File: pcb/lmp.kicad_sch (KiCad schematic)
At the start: 6 parts, among them J2 Conn_01x03, J5 TB003-500-P03BE, J6 Conn_01x03_Pin, U2 LMP91000SDX/NOPB

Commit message: Simplify to minimum buck converter components
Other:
- title: (none) -> LMP91000 Portable Potentiostat
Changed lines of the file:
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@@
 	(generator_version "9.0")
 	(paper "A4")
+	(title_block
+		(title "LMP91000 Portable Potentiostat")
+	)
 	(text "Label these with silkscreen"
 		(exclude_from_sim no)

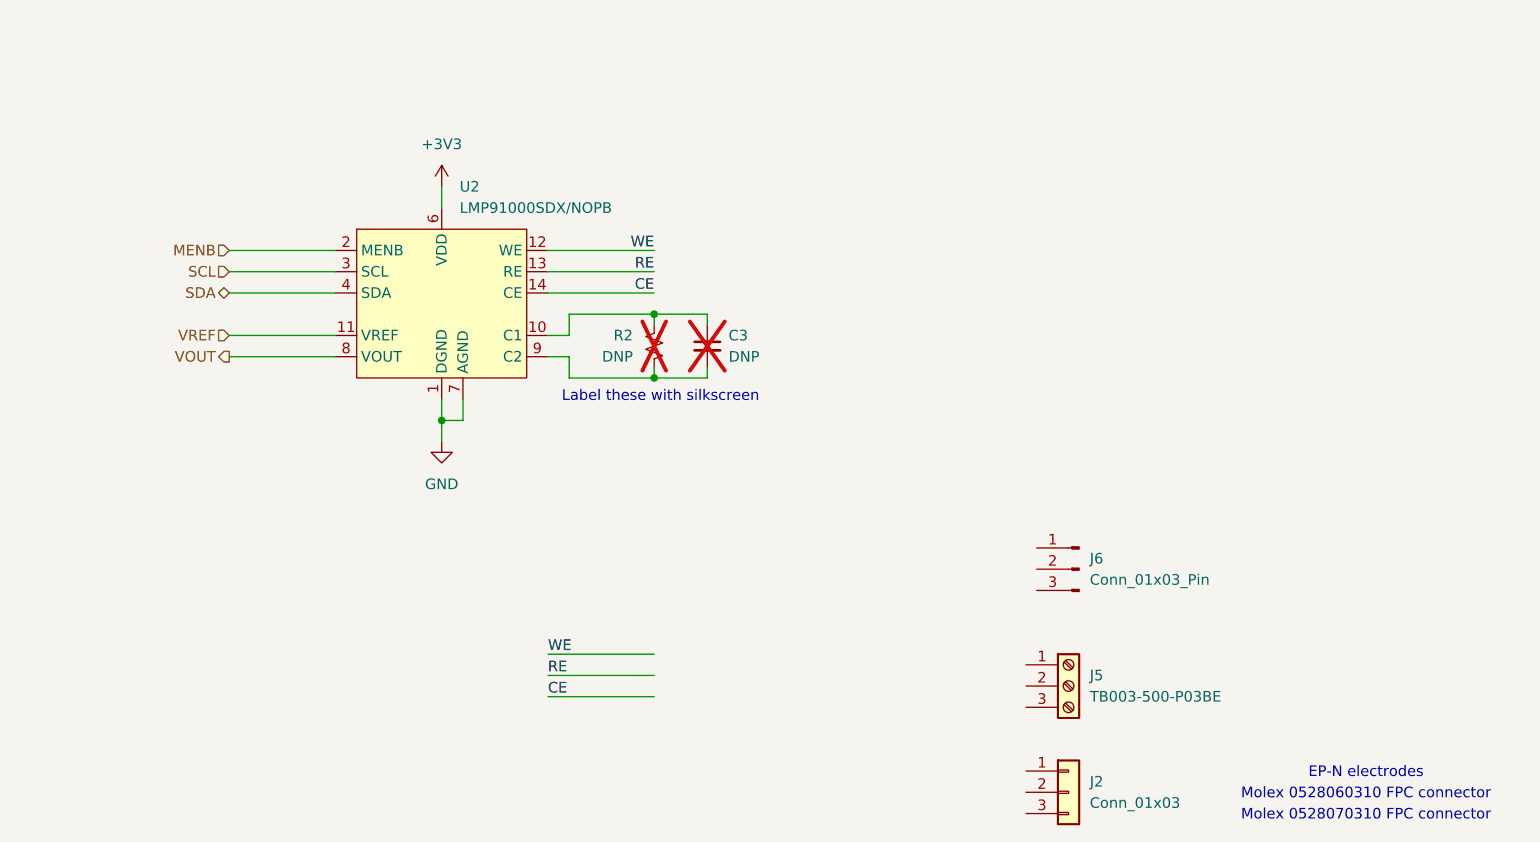
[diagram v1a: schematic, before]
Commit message: Assign footprints, cleanup schematics, start layout
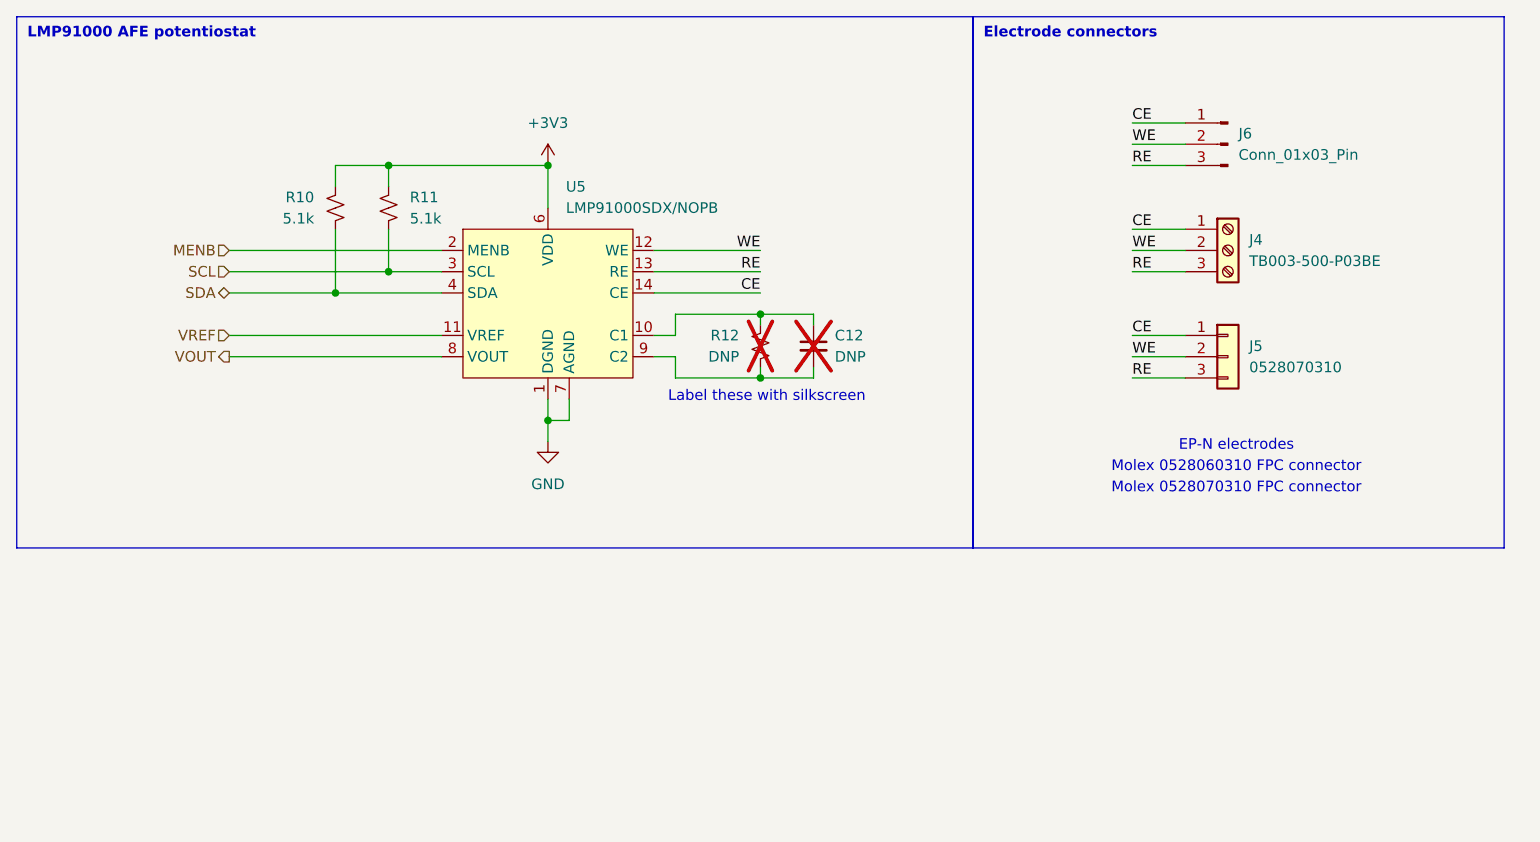
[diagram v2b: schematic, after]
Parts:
- added R10, R11: 5.1k, Resistor_SMD:R_0402_1005Metric, symbol Device:R_Small_US
- C12: renamed from C3; footprint (none) -> Capacitor_SMD:C_0805_2012Metric
- J4: renamed from J5; footprint (none) -> TerminalBlock_SameSky:CUI_TB003-500-P03BE
- J5: renamed from J2; value Conn_01x03 -> 0528070310; footprint (none) -> Connector_Molex_Easy-On:528070310
- J6: footprint (none) -> Connector_PinHeader_2.54mm:PinHeader_1x03_P2.54mm_Vertical; now left out of the parts list
- R12: renamed from R2; footprint (none) -> Resistor_SMD:R_0805_2012Metric
- renumbered U2 to U5
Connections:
- net +3V3: now also R10.2, R11.2
- net CE: now also J4.1 (Pin_1), J5.1 (Pin_1), J6.1 (Pin_1)
- net RE: now also J4.3 (Pin_3), J5.3 (Pin_3), J6.3 (Pin_3)
- net SCL: now also R11.1
- net SDA: now also R10.1
- net WE: now also J4.2 (Pin_2), J5.2 (Pin_2), J6.2 (Pin_2)
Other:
- note added: "Electrode connectors"
- note added: "LMP91000 AFE potentiostat"
- company: (none) -> Clarkson University
- moved on the sheet: C12, J4, J5, J6, R12, U5

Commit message: Finish PCB
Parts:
- C12: footprint Capacitor_SMD:C_0805_2012Metric -> Capacitor_SMD:C_0603_1608Metric_Pad1.08x0.95mm_HandSolder
- J4: value TB003-500-P03BE -> TB0011-350-03GR; footprint TerminalBlock_SameSky:CUI_TB003-500-P03BE -> TerminalBlock_SameSky:SAMESKY_TB0011-350-03GR
- J6: now not fitted
- R12: footprint Resistor_SMD:R_0805_2012Metric -> Resistor_SMD:R_0603_1608Metric_Pad0.98x0.95mm_HandSolder
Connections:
- net CE: now also J4.3 (Pin_3); no longer J4.1 (Pin_1)
- net RE: now also J4.1 (Pin_1); no longer J4.3 (Pin_3)
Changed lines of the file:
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@@
 			)
 		)
-		(property "Footprint" "Resistor_SMD:R_0805_2012Metric"
+		(property "Footprint" "Resistor_SMD:R_0603_1608Metric_Pad0.98x0.95mm_HandSolder"
 			(at 101.6 52.07 0)
 			(effects
@@
 		(lib_id "Connector:Screw_Terminal_01x03")
 		(at 157.48 40.64 0)
+		(mirror x)
 		(unit 1)
 		(exclude_from_sim no)
@@
 		(on_board yes)
 		(dnp no)
-		(fields_autoplaced yes)
 		(property "Reference" "J4"
-			(at 160.02 39.3699 0)
-			(effects
-				(font
-					(size 1.27 1.27)
-				)
-				(justify left)
-			)
-		)
-		(property "Value" "TB003-500-P03BE"
-			(at 160.02 41.9099 0)
-			(effects
-				(font
-					(size 1.27 1.27)
-				)
-				(justify left)
-			)
-		)
-		(property "Footprint" "TerminalBlock_SameSky:CUI_TB003-500-P03BE"
+			(at 160.02 41.9101 0)
+			(effects
+				(font
+					(size 1.27 1.27)
+				)
+				(justify left)
+			)
+		)
+		(property "Value" "TB0011-350-03GR"
+			(at 160.02 39.3701 0)
+			(effects
+				(font
+					(size 1.27 1.27)
+				)
+				(justify left)
+			)
+		)
+		(property "Footprint" "TerminalBlock_SameSky:SAMESKY_TB0011-350-03GR"
 			(at 157.48 40.64 0)
 			(effects
@@
 		(exclude_from_sim no)
 		(in_bom no)
-		(on_board yes)
-		(dnp no)
+		(on_board no)
+		(dnp yes)
 		(fields_autoplaced yes)
 		(property "Reference" "J6"
@@
 			)
 		)
-		(property "Footprint" "Capacitor_SMD:C_0805_2012Metric"
+		(property "Footprint" "Capacitor_SMD:C_0603_1608Metric_Pad1.08x0.95mm_HandSolder"
 			(at 107.95 52.07 0)
 			(effects

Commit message: Move antenna and tag connect
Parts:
- C12, R12: now left out of the parts list
- J4: HQ_MPN (none) -> TB0011-350-03GR
- J5: HQ_MPN (none) -> 0528070310
- R10, R11: HQ_MPN (none) -> WR04X5101FTL
- U5: HQ_MPN (none) -> LMP91000SDX/NOPB
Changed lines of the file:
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@@
 		(unit 1)
 		(exclude_from_sim no)
-		(in_bom yes)
+		(in_bom no)
 		(on_board yes)
 		(dnp yes)
@@
 			)
 		)
+		(property "HQ_MPN" ""
+			(at 101.6 52.07 0)
+			(effects
+				(font
+					(size 1.27 1.27)
+				)
+				(hide yes)
+			)
+		)
 		(pin "2"
 		)
@@
 			)
 		)
+		(property "HQ_MPN" "WR04X5101FTL"
+			(at 57.15 35.56 0)
+			(effects
+				(font
+					(size 1.27 1.27)
+				)
+				(hide yes)
+			)
+		)
 		(pin "2"
 		)
@@
 		)
 		(property "Description" "Generic screw terminal, single row, 01x03, script generated (kicad-library-utils/schlib/autogen/connector/)"
+			(at 157.48 40.64 0)
+			(effects
+				(font
+					(size 1.27 1.27)
+				)
+				(hide yes)
+			)
+		)
+		(property "HQ_MPN" "TB0011-350-03GR"
 			(at 157.48 40.64 0)
 			(effects
@@
 			)
 		)
+		(property "HQ_MPN" ""
+			(at 157.48 27.94 0)
+			(effects
+				(font
+					(size 1.27 1.27)
+				)
+				(hide yes)
+			)
+		)
 		(pin "3"
 		)
@@
 			)
 		)
+		(property "HQ_MPN" "0528070310"
+			(at 157.48 53.34 0)
+			(effects
+				(font
+					(size 1.27 1.27)
+				)
+				(hide yes)
+			)
+		)
 		(pin "1"
 		)
@@
 			)
 		)
+		(property "HQ_MPN" "LMP91000SDX/NOPB"
+			(at 76.2 38.1 0)
+			(effects
+				(font
+					(size 1.27 1.27)
+				)
+				(hide yes)
+			)
+		)
 		(pin "15"
 		)
@@
 		(unit 1)
 		(exclude_from_sim no)
-		(in_bom yes)
+		(in_bom no)
 		(on_board yes)
 		(dnp yes)
@@
 			)
 		)
+		(property "HQ_MPN" ""
+			(at 107.95 52.07 0)
+			(effects
+				(font
+					(size 1.27 1.27)
+				)
+				(hide yes)
+			)
+		)
 		(pin "2"
 		)
@@
 			(at 50.8 35.56 0)
 			(effects
+				(font
+					(size 1.27 1.27)
+				)
+				(hide yes)
+			)
+		)
+		(property "HQ_MPN" "WR04X5101FTL"
+			(at 50.8 35.56 0)
+			(effects

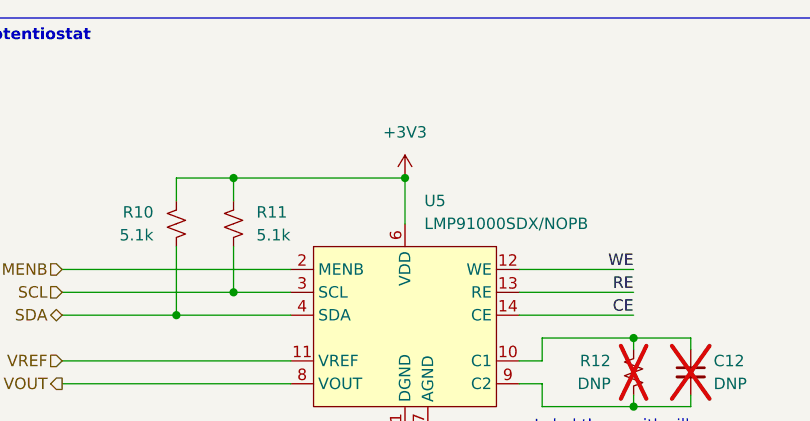
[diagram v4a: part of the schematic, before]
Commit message: Create Simplicity Studio 6 firmware project
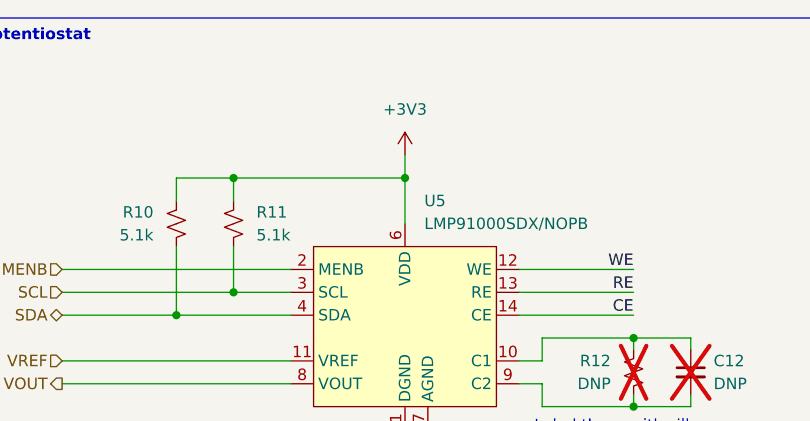
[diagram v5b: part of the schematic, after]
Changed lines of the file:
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@@
+	(wire
+		(pts
+			(xy 76.2 27.94) (xy 76.2 30.48)
+		)
+		(stroke
+			(width 0)
+			(type default)
+		)
+	)
 	(wire
 		(pts
@@
 	(symbol
 		(lib_id "power:+3V3")
-		(at 76.2 30.48 0)
+		(at 76.2 27.94 0)
 		(unit 1)
 		(exclude_from_sim no)
@@
 		(fields_autoplaced yes)
 		(property "Reference" "#PWR032"
-			(at 76.2 34.29 0)
+			(at 76.2 31.75 0)
 			(effects
 				(font
@@
 		)
 		(property "Value" "+3V3"
-			(at 76.2 25.4 0)
+			(at 76.2 22.86 0)
 			(effects
 				(font
@@
 		)
 		(property "Footprint" ""
-			(at 76.2 30.48 0)
+			(at 76.2 27.94 0)
 			(effects
 				(font
@@
 		)
 		(property "Datasheet" ""
-			(at 76.2 30.48 0)
+			(at 76.2 27.94 0)
 			(effects
 				(font
@@
 		)
 		(property "Description" "Power symbol creates a global label with name \"+3V3\""
-			(at 76.2 30.48 0)
+			(at 76.2 27.94 0)
 			(effects
 				(font
